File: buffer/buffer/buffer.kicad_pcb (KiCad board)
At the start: 2 copper layers, 16.5 x 10.5 mm, 8 parts, among them J1 in, J2 VDD, J3 VSS, J4 out, P1 P, P2 P

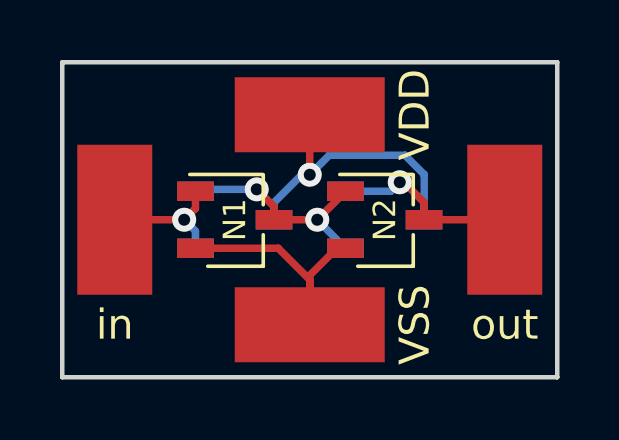
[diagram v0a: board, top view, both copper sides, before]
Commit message: Fixed a broken circuit
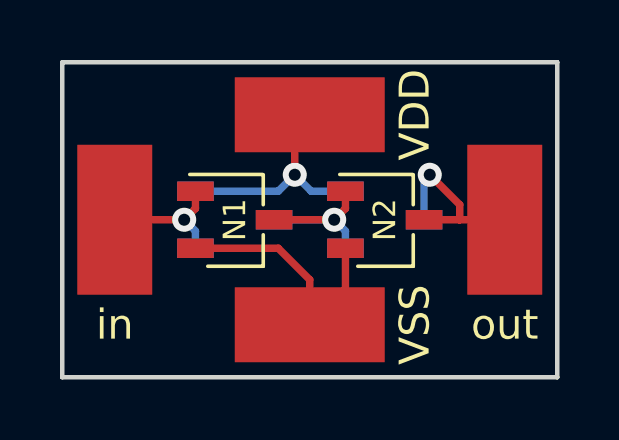
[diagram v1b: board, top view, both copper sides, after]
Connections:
- P1 pad 2: /Buffer_1/Inv_2/in -> VDD
- P1 pad 3: VDD -> /Buffer_1/Inv_2/in
- P2 pad 2: /Buffer_1/out -> VDD
- P2 pad 3: VDD -> /Buffer_1/out
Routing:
- net VDD: track 10.0 -> 7.66 mm
- net /Buffer_1/Inv_2/in: track 7.44 -> 6.22 mm, vias 2 -> 1
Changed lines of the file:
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@@
     (thickness 1.6)
     (drawings 5)
-    (tracks 41)
+    (tracks 32)
     (zones 0)
     (modules 8)
@@
       (net 1 /Buffer_1/in))
     (pad 2 smd rect (at -1.31 -0.95) (size 1.22 0.65) (layers B.Cu B.Paste B.Mask)
+      (net 2 VDD))
+    (pad 3 smd rect (at 1.31 0) (size 1.22 0.65) (layers B.Cu B.Paste B.Mask)
       (net 5 /Buffer_1/Inv_2/in))
-    (pad 3 smd rect (at 1.31 0) (size 1.22 0.65) (layers B.Cu B.Paste B.Mask)
-      (net 2 VDD))
     (model ${KISYS3DMOD}/TO_SOT_Packages_SMD.3dshapes/TSOT-23.wrl
       (at (xyz 0 0 0))
@@
       (net 5 /Buffer_1/Inv_2/in))
     (pad 2 smd rect (at -1.31 -0.95) (size 1.22 0.65) (layers B.Cu B.Paste B.Mask)
+      (net 2 VDD))
+    (pad 3 smd rect (at 1.31 0) (size 1.22 0.65) (layers B.Cu B.Paste B.Mask)
       (net 4 /Buffer_1/out))
-    (pad 3 smd rect (at 1.31 0) (size 1.22 0.65) (layers B.Cu B.Paste B.Mask)
-      (net 2 VDD))
     (model ${KISYS3DMOD}/TO_SOT_Packages_SMD.3dshapes/TSOT-23.wrl
       (at (xyz 0 0 0))
@@
   (segment (start 157.315 116) (end 157.69 115.625) (width 0.25) (layer F.Cu) (net 1))
   (segment (start 157.69 115.625) (end 157.69 115.05) (width 0.25) (layer F.Cu) (net 1))
-  (segment (start 161.235 114.5) (end 161.50001 114.5) (width 0.25) (layer B.Cu) (net 2))
-  (segment (start 160.31 115.425) (end 161.235 114.5) (width 0.25) (layer B.Cu) (net 2))
-  (segment (start 160.31 116) (end 160.31 115.425) (width 0.25) (layer B.Cu) (net 2))
-  (segment (start 161.900009 114.100001) (end 161.50001 114.5) (width 0.25) (layer B.Cu) (net 2))
-  (segment (start 162.150008 113.850002) (end 161.900009 114.100001) (width 0.25) (layer B.Cu) (net 2))
-  (segment (start 164.673008 113.850002) (end 162.150008 113.850002) (width 0.25) (layer B.Cu) (net 2))
-  (segment (start 165.31 116) (end 165.31 114.486994) (width 0.25) (layer B.Cu) (net 2))
-  (segment (start 165.31 114.486994) (end 164.673008 113.850002) (width 0.25) (layer B.Cu) (net 2))
-  (segment (start 161.5 112.5) (end 161.5 114.49999) (width 0.25) (layer F.Cu) (net 2))
-  (segment (start 161.5 114.49999) (end 161.50001 114.5) (width 0.25) (layer F.Cu) (net 2))
-  (via (at 161.50001 114.5) (size 0.8) (drill 0.4) (layers F.Cu B.Cu) (net 2))
-  (segment (start 161.5 119.5) (end 161.5 117.855) (width 0.25) (layer F.Cu) (net 3))
-  (segment (start 161.5 117.855) (end 162.405 116.95) (width 0.25) (layer F.Cu) (net 3))
-  (segment (start 162.405 116.95) (end 162.69 116.95) (width 0.25) (layer F.Cu) (net 3))
+  (segment (start 157.69 115.05) (end 160.45 115.05) (width 0.25) (layer B.Cu) (net 2))
+  (segment (start 160.45 115.05) (end 161 114.5) (width 0.25) (layer B.Cu) (net 2))
+  (segment (start 161 114.5) (end 161 113) (width 0.25) (layer F.Cu) (net 2))
+  (segment (start 161 113) (end 161.5 112.5) (width 0.25) (layer F.Cu) (net 2))
+  (segment (start 162.69 115.05) (end 161.55 115.05) (width 0.25) (layer B.Cu) (net 2))
+  (via (at 161 114.5) (size 0.8) (drill 0.4) (layers F.Cu B.Cu) (net 2))
+  (segment (start 161.55 115.05) (end 161 114.5) (width 0.25) (layer B.Cu) (net 2))
   (segment (start 157.69 116.95) (end 160.45 116.95) (width 0.25) (layer F.Cu) (net 3))
   (segment (start 160.45 116.95) (end 161.5 118) (width 0.25) (layer F.Cu) (net 3))
   (segment (start 161.5 118) (end 161.5 119.5) (width 0.25) (layer F.Cu) (net 3))
-  (segment (start 164.635003 114.750003) (end 164.499997 114.750003) (width 0.25) (layer F.Cu) (net 4))
-  (segment (start 165.31 116) (end 165.31 115.425) (width 0.25) (layer F.Cu) (net 4))
-  (segment (start 165.31 115.425) (end 164.635003 114.750003) (width 0.25) (layer F.Cu) (net 4))
-  (segment (start 162.69 115.05) (end 164.2 115.05) (width 0.25) (layer B.Cu) (net 4))
-  (via (at 164.499997 114.750003) (size 0.8) (drill 0.4) (layers F.Cu B.Cu) (net 4))
-  (segment (start 164.2 115.05) (end 164.499997 114.750003) (width 0.25) (layer B.Cu) (net 4))
-  (segment (start 165.31 116) (end 168 116) (width 0.25) (layer F.Cu) (net 4))
-  (segment (start 160.31 116) (end 161.75 116) (width 0.25) (layer F.Cu) (net 5))
-  (segment (start 161.75 116) (end 161.75 116.01) (width 0.25) (layer B.Cu) (net 5))
-  (segment (start 161.75 116.01) (end 162.69 116.95) (width 0.25) (layer B.Cu) (net 5))
-  (segment (start 162.69 115.05) (end 162.69 115.06) (width 0.25) (layer F.Cu) (net 5))
-  (segment (start 162.69 115.06) (end 161.75 116) (width 0.25) (layer F.Cu) (net 5))
-  (via (at 161.75 116) (size 0.8) (drill 0.4) (layers F.Cu B.Cu) (net 5))
-  (segment (start 159.732484 114.986707) (end 157.753293 114.986707) (width 0.25) (layer B.Cu) (net 5))
-  (segment (start 157.753293 114.986707) (end 157.69 115.05) (width 0.25) (layer B.Cu) (net 5))
-  (segment (start 160.31 116) (end 160.31 115.564223) (width 0.25) (layer F.Cu) (net 5))
-  (segment (start 160.31 115.564223) (end 159.732484 114.986707) (width 0.25) (layer F.Cu) (net 5))
-  (via (at 159.732484 114.986707) (size 0.8) (drill 0.4) (layers F.Cu B.Cu) (net 5))
+  (segment (start 162.69 116.95) (end 162.69 118.31) (width 0.25) (layer F.Cu) (net 3))
+  (segment (start 162.69 118.31) (end 161.5 119.5) (width 0.25) (layer F.Cu) (net 3))
+  (segment (start 165.31 116) (end 166.5 116) (width 0.25) (layer F.Cu) (net 4))
+  (segment (start 166.5 116) (end 168 116) (width 0.25) (layer F.Cu) (net 4))
+  (segment (start 165.5 114.5) (end 166.5 115.5) (width 0.25) (layer F.Cu) (net 4))
+  (segment (start 166.5 115.5) (end 166.5 116) (width 0.25) (layer F.Cu) (net 4))
+  (segment (start 165.31 116) (end 165.31 114.69) (width 0.25) (layer B.Cu) (net 4))
+  (via (at 165.5 114.5) (size 0.8) (drill 0.4) (layers F.Cu B.Cu) (net 4))
+  (segment (start 165.31 114.69) (end 165.5 114.5) (width 0.25) (layer B.Cu) (net 4))
+  (segment (start 160.31 116) (end 162.315 116) (width 0.25) (layer B.Cu) (net 5))
+  (segment (start 162.69 116.95) (end 162.69 116.375) (width 0.25) (layer B.Cu) (net 5))
+  (segment (start 162.69 116.375) (end 162.315 116) (width 0.25) (layer B.Cu) (net 5))
+  (via (at 162.315 116) (size 0.8) (drill 0.4) (layers F.Cu B.Cu) (net 5))
+  (segment (start 160.31 116) (end 162.315 116) (width 0.25) (layer F.Cu) (net 5))
+  (segment (start 162.315 116) (end 162.69 115.625) (width 0.25) (layer F.Cu) (net 5))
+  (segment (start 162.69 115.625) (end 162.69 115.05) (width 0.25) (layer F.Cu) (net 5))
 )
